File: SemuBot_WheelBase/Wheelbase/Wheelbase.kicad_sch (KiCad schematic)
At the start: 50 parts, among them J1 10155435-00011LF, J10 B5B-XH-A_LF__SN_, J11 B5B-XH-A_LF__SN_, J12 B5B-XH-A_LF__SN_, J13 MTSW-104-09-L-S-400, J14 XT30PW-M, J15 MTSW-104-09-L-S-400, J2 MTSW-102-09-L-S-400, J3 MR30PW-M, J4 B5B-XH-A_LF__SN_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

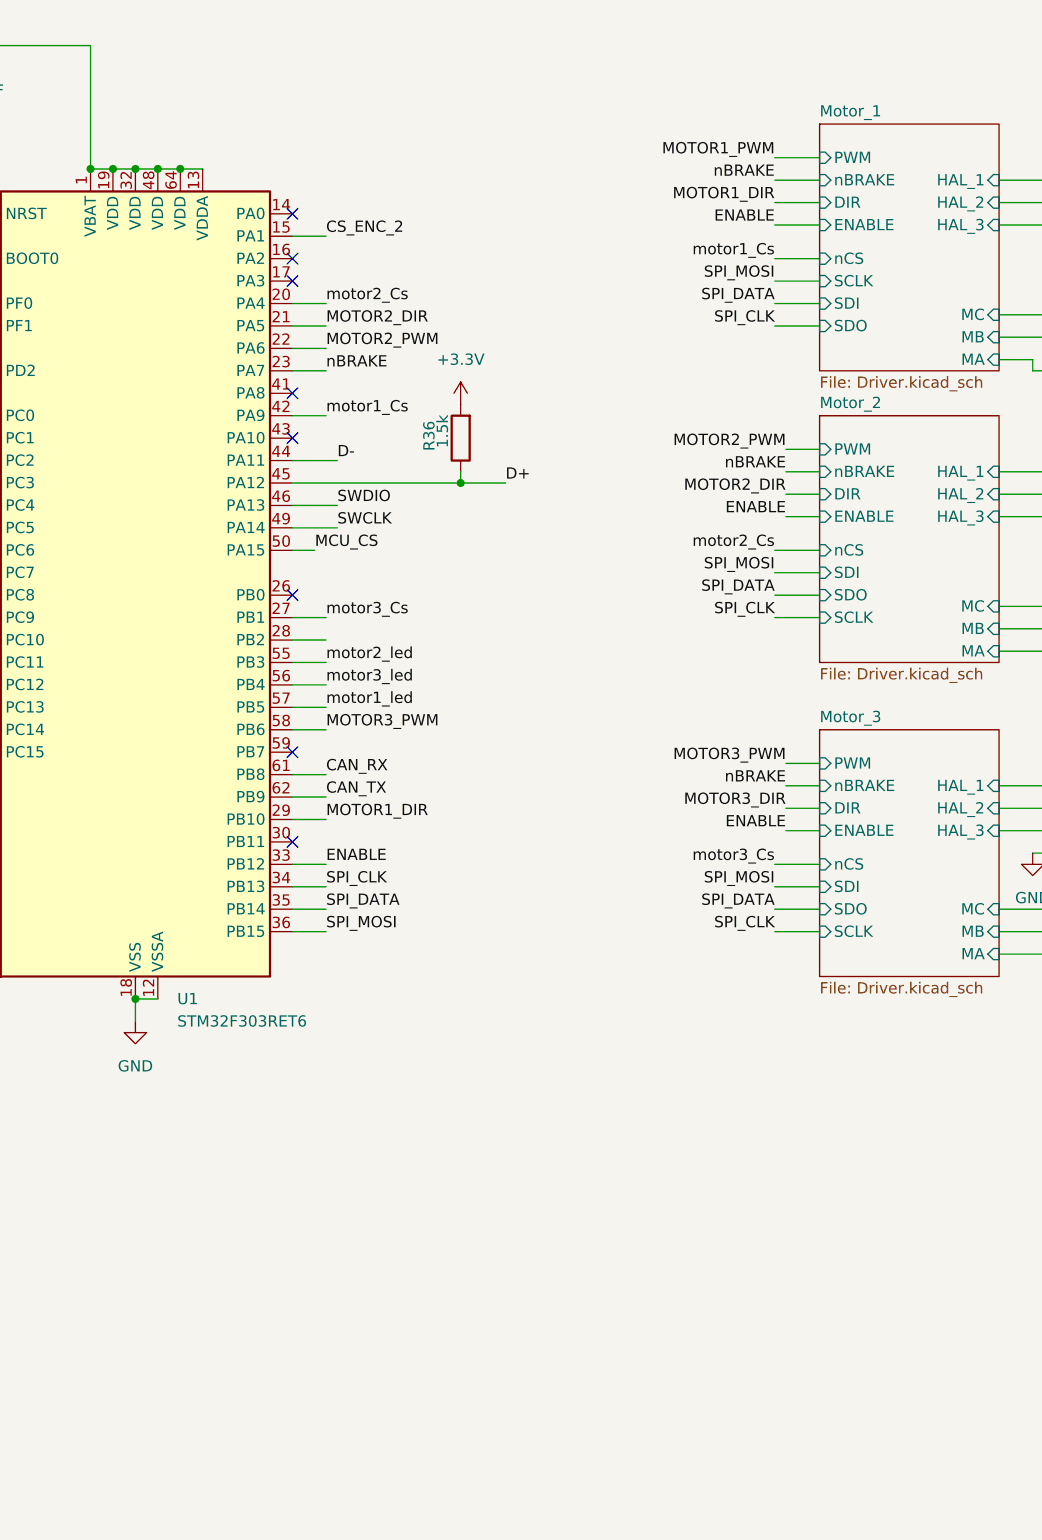
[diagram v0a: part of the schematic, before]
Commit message: Wheelbase development and repo cleanup
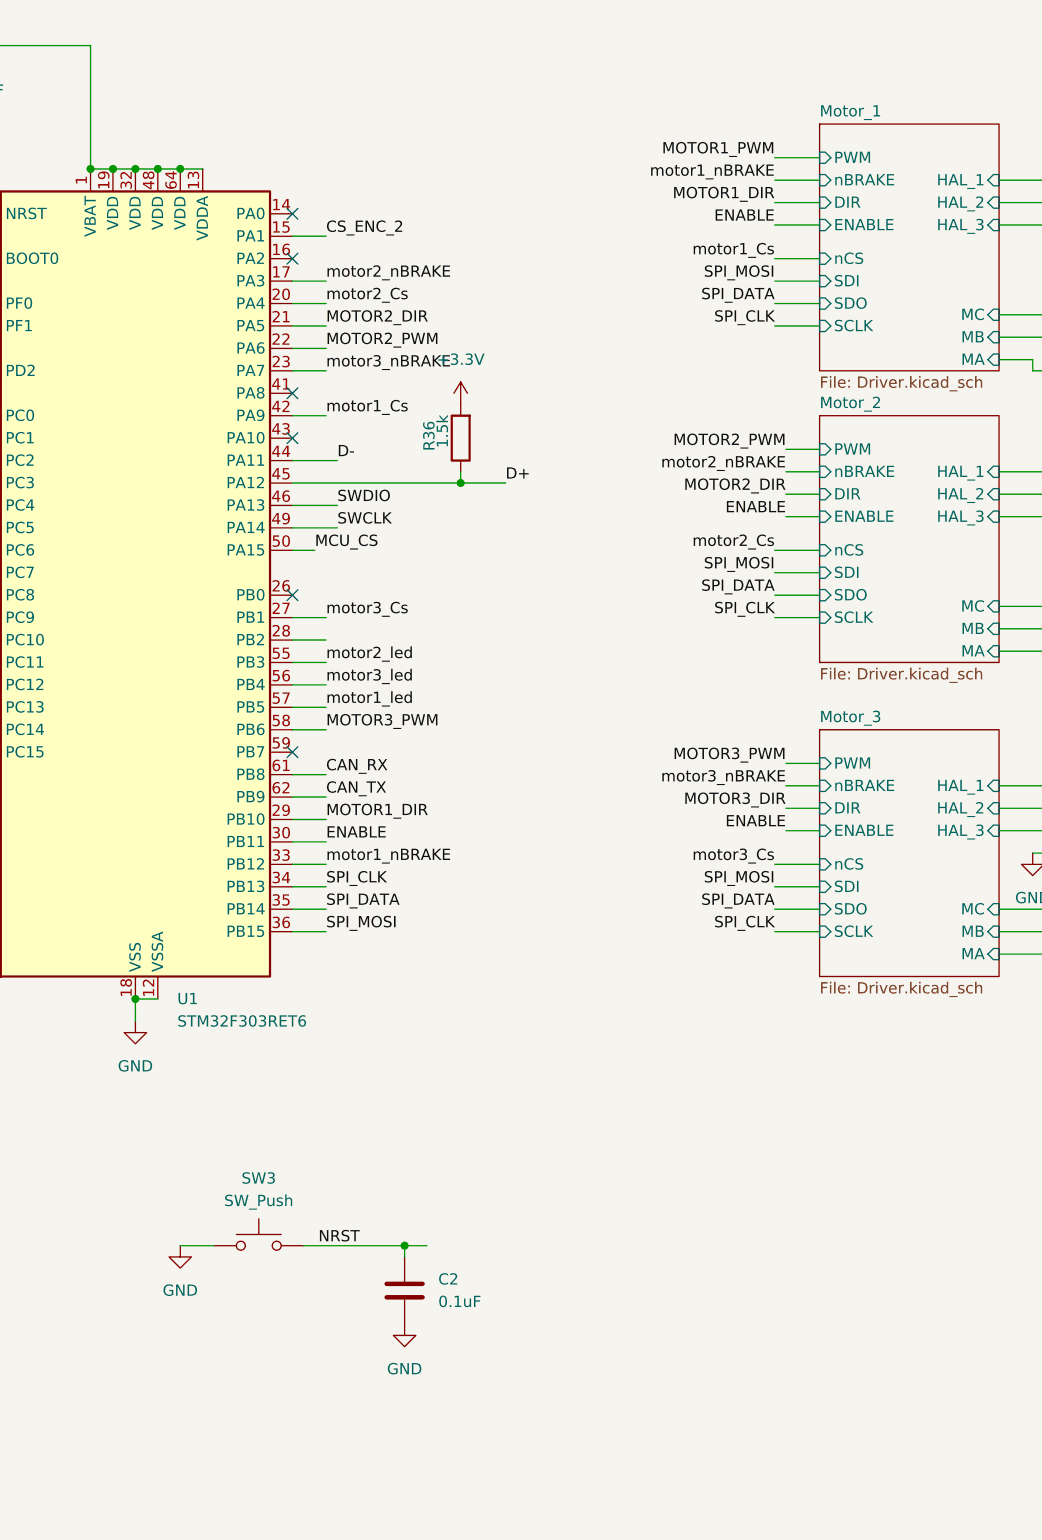
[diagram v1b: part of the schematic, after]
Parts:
- added C2: 0.1uF, Capacitor_SMD:C_0603_1608Metric_Pad1.08x0.95mm_HandSolder, symbol Device:C
- added SW3: SW_Push, symbol Switch:SW_Push
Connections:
- net ENABLE: now also U1.30 (PB11); no longer U1.33 (PB12)
- net GND: now also C2.2, SW3.1
- net NRST: now also C2.1, SW3.2
- net motor2_nBRAKE: now reaches U1.17 (PA3)
- net nBRAKE renamed motor3_nBRAKE
- new net motor1_nBRAKE: U1.33 (PB12)
- no-connect marks 22 -> 20

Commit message: Current sensing
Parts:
- removed C2: 0.1uF, Capacitor_SMD:C_0603_1608Metric_Pad1.08x0.95mm_HandSolder, symbol Device:C
- removed D10, D11, D12: red, LED_SMD:LED_0603_1608Metric_Pad1.05x0.95mm_HandSolder, symbol Device:LED
- removed R21, R22, R23: 3.3K, Resistor_SMD:R_0603_1608Metric_Pad0.98x0.95mm_HandSolder, symbol Device:R
- removed SW3: SW_Push, symbol Switch:SW_Push
- added C50: 100nF, Capacitor_SMD:C_0603_1608Metric_Pad1.08x0.95mm_HandSolder, symbol Device:C
- added R45: 3.3K, Resistor_SMD:R_0603_1608Metric_Pad0.98x0.95mm_HandSolder, symbol Device:R
- added Y1: ECS-2520MVLC-081.92-CN-TR, ECS-2520:OSC_ECS-2520MVLC-081.92-CN-TR, symbol ECS-2520MVLC-081.92-CN-TR:ECS-2520MVLC-081.92-CN-TR
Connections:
- net +3.3V: now also C50.1, Y1.1 (TRI_STATE), Y1.4 (VDD)
- net +5V: now also R45.2
- net CS_ENC_1: now also U1.39 (PC8); no longer U1.38 (PC7)
- net CS_ENC_3: now also U1.38 (PC7); no longer U1.37 (PC6)
- net GND: now also C50.2, Y1.2 (GND)
- net MOTOR1_DIR: now also U1.37 (PC6); no longer U1.29 (PB10)
- net MOTOR1_PWM: now also U1.41 (PA8); no longer U1.8 (PC0)
- net Motor_1/HAL_1: now also J4.4; no longer J4.2
- net Motor_1/HAL_3: now also J4.2; no longer J4.4
- net SPI_DATA: now also R45.1
- net motor2_DRDY: now reaches U1.14 (PA0)
- net motor2_adc: now reaches U1.16 (PA2)
- net motor3_adc: now reaches U1.28 (PB2)
- net motor1_DRDY: now reaches U1.40 (PC9)
- net motor1_adc: now reaches U1.43 (PA10)
- net motor1_led: no longer names the net of U1.57 (PB5)
- net motor2_led: no longer names the net of U1.55 (PB3)
- net motor3_led: no longer names the net of U1.56 (PB4)
- new net adc_CLK: Y1.3 (OUTPUT)
- new net motor3_DRDY: U1.29 (PB10)
- no-connect marks 20 -> 18
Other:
- sheet Motor_1 ports: added ADC_CS, DRDY, adc_CLK; removed none
- sheet Motor_2 ports: added ADC_CS, DRDY, adc_CLK; removed none
- sheet Motor_3 ports: added ADC_CS, DRDY, adc_CLK; removed none
- note removed: "Debug Leds"
- moved on the sheet: J5, J6, J7, J8

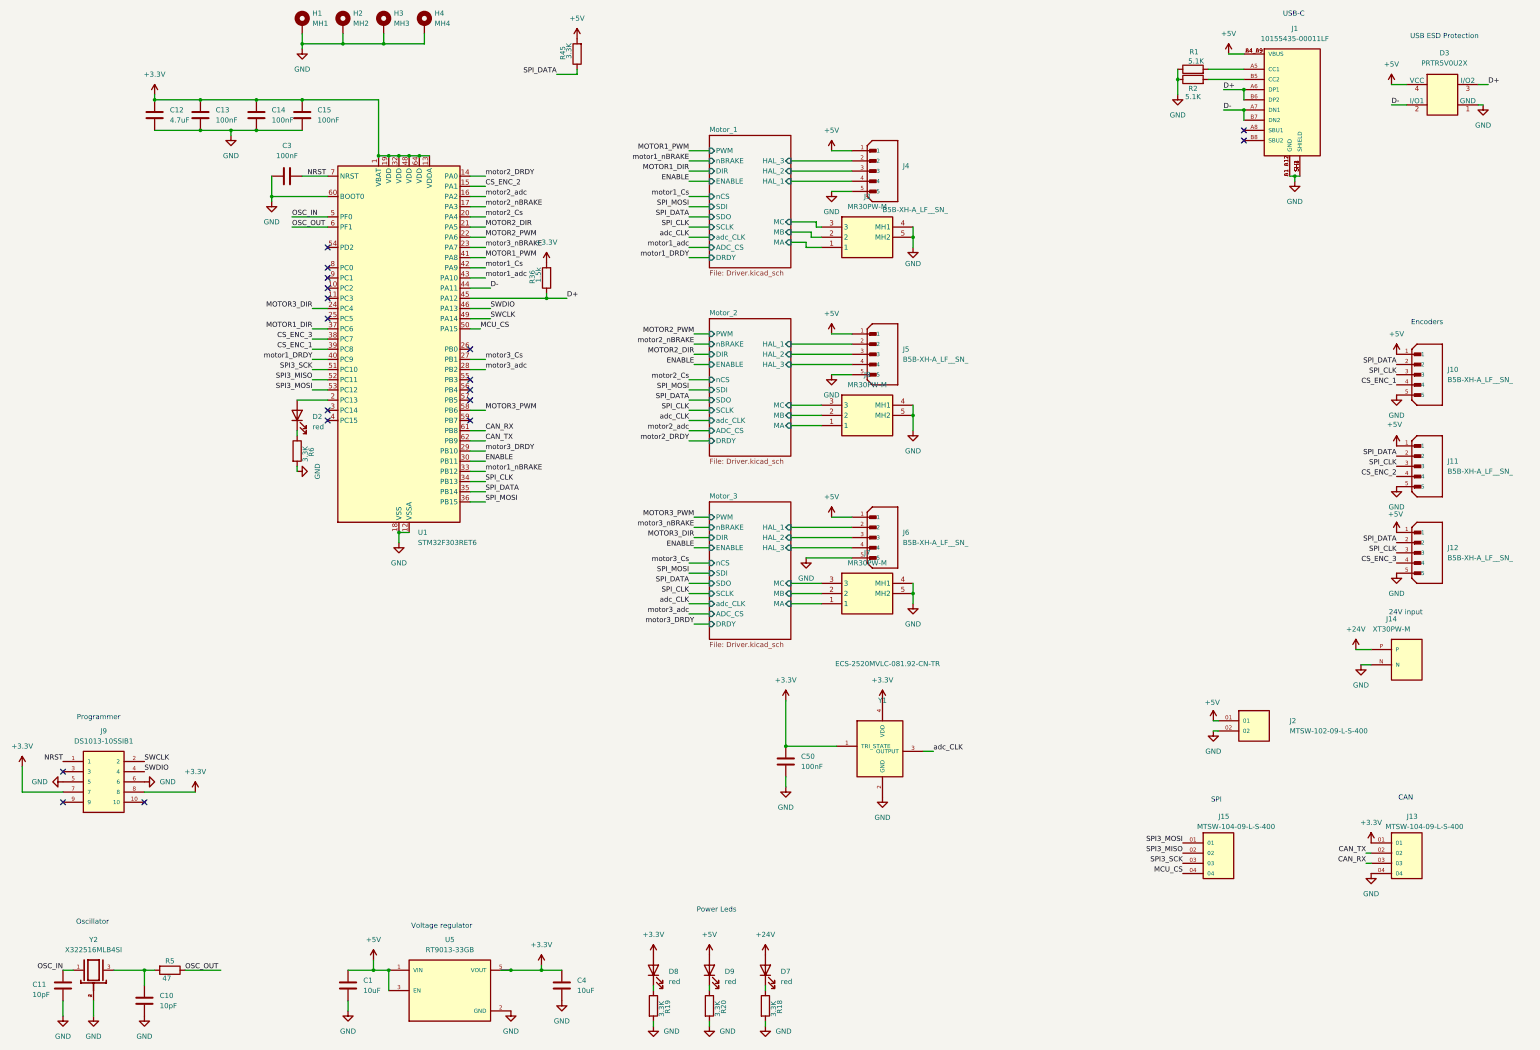
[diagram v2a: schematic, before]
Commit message: Current sensing, + changing encoder pins
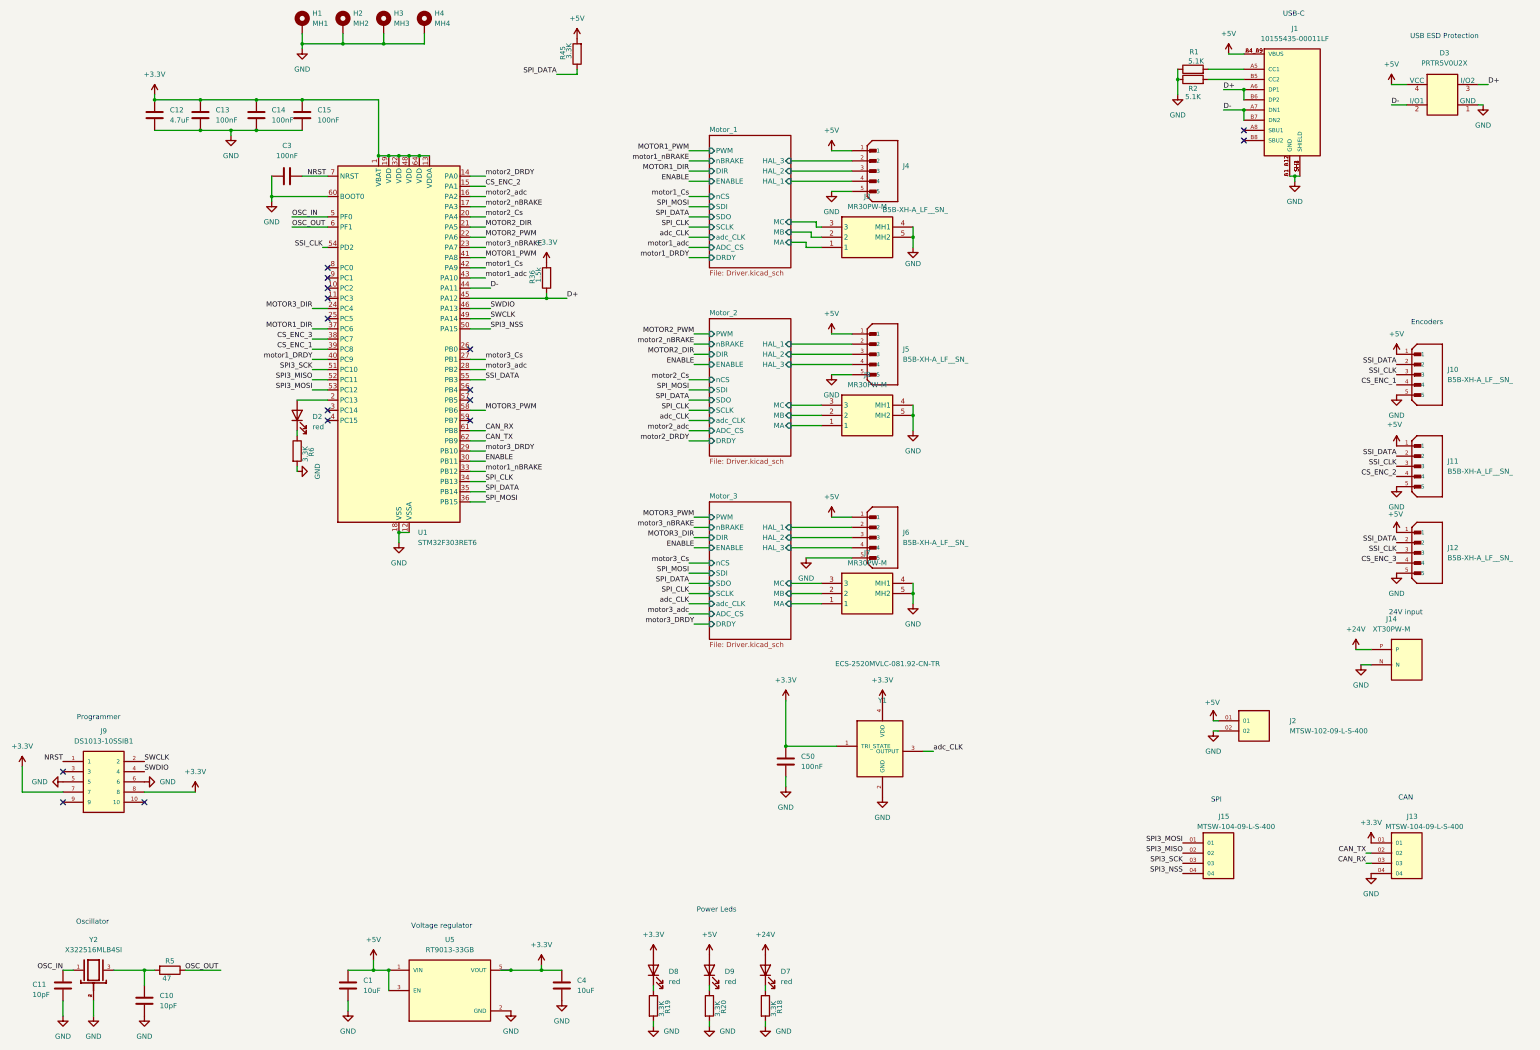
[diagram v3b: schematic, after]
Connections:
- net SPI_CLK: no longer J10.3, J11.3, J12.3
- net SPI_DATA: no longer J10.2, J11.2, J12.2
- net SSI_CLK: now reaches U1.54 (PD2)
- net SSI_CLK: now also J10.3, J11.3, J12.3
- net SSI_DATA: now reaches U1.55 (PB3)
- net SSI_DATA: now also J10.2, J11.2, J12.2
- net MCU_CS renamed SPI3_NSS
- no-connect marks 18 -> 16
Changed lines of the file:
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@@
-	)
-	(no_connect
-		(at 100.33 77.47)
 	)
 	(no_connect
@@
 	)
 	(no_connect
-		(at 135.89 110.49)
-	)
-	(no_connect
 		(at 100.33 90.17)
 	)
@@
 	(wire
 		(pts
-			(xy 135.89 97.79) (xy 138.43 97.79)
+			(xy 135.89 97.79) (xy 140.97 97.79)
 		)
 		(stroke
@@
 	(wire
 		(pts
+			(xy 99.06 77.47) (xy 100.33 77.47)
+		)
+		(stroke
+			(width 0)
+			(type default)
+		)
+	)
+	(wire
+		(pts
 			(xy 140.97 92.71) (xy 135.89 92.71)
 		)
@@
 		(pts
 			(xy 215.9 101.6) (xy 231.14 101.6)
+		)
+		(stroke
+			(width 0)
+			(type default)
+		)
+	)
+	(wire
+		(pts
+			(xy 139.7 110.49) (xy 135.89 110.49)
 		)
 		(stroke
@@
 		)
 	)
-	(label "MCU_CS"
+	(label "SPI3_NSS"
 		(at 313.69 233.68 180)
 		(effects
@@
 		)
 	)
-	(label "SPI_DATA"
+	(label "SSI_DATA"
 		(at 367.03 129.54 180)
 		(effects
@@
 		)
 	)
+	(label "SSI_CLK"
+		(at 99.06 77.47 180)
+		(effects
+			(font
+				(size 1.27 1.27)
+			)
+			(justify right bottom)
+		)
+	)
 	(label "motor1_Cs"
 		(at 139.7 82.55 0)
@@
 		)
 	)
+	(label "SSI_DATA"
+		(at 139.7 110.49 0)
+		(effects
+			(font
+				(size 1.27 1.27)
+			)
+			(justify left bottom)
+		)
+	)
 	(label "motor3_Cs"
 		(at 139.7 105.41 0)
@@
 		)
 	)
-	(label "SPI_CLK"
+	(label "SSI_CLK"
 		(at 367.03 132.08 180)
 		(effects
@@
 		)
 	)
-	(label "MCU_CS"
-		(at 138.43 97.79 0)
+	(label "SPI3_NSS"
+		(at 140.97 97.79 0)
 		(effects
 			(font
@@
 		)
 	)
-	(label "SPI_CLK"
+	(label "SSI_CLK"
 		(at 367.03 109.22 180)
 		(effects
@@
 		)
 	)
-	(label "SPI_DATA"
+	(label "SSI_DATA"
 		(at 367.03 106.68 180)
 		(effects
@@
 		)
 	)
-	(label "SPI_CLK"
+	(label "SSI_CLK"
 		(at 367.03 153.67 180)
 		(effects
@@
 		)
 	)
-	(label "SPI_DATA"
+	(label "SSI_DATA"
 		(at 367.03 151.13 180)
 		(effects
